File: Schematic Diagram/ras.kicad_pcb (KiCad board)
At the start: 2 copper layers, 1 part

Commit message: display parts
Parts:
- added BZ1: Buzzer, project:Buzzer_12x9.5RM7.6, F.Cu at (159.2, 32.4)
- added D1: LED_RED, project:LED_D5.0mm, F.Cu at (161.7, 54.7)
- added D2: LED_GREEN, project:LED_D5.0mm, F.Cu at (161.7, 48.3)
- added D3: LED_BLUE, project:LED_D5.0mm, F.Cu at (161.7, 41.9)
- added LCD_Module1: I2C_transport_LCD, project:WC1602A, F.Cu at (181.0, 27.4)
- added R1: 130Ω, project:R_Axial_DIN0207_L6.3mm_D2.5mm_P7.62mm_Horizontal, F.Cu at (170.8, 60.1)
- added R2: 130Ω, project:R_Axial_DIN0207_L6.3mm_D2.5mm_P7.62mm_Horizontal, F.Cu at (167.8, 60.1)
- added R3: 130Ω, project:R_Axial_DIN0207_L6.3mm_D2.5mm_P7.62mm_Horizontal, F.Cu at (164.8, 60.1)
- added RFID1: RC522, project:RFID-RC522, F.Cu at (241.7, 77.2)
- added SW1: SHUTDOWN, project:SW_PUSH_6mm, F.Cu at (156.8, 67.2)
- added SW2: HOME, project:SW_PUSH_6mm, F.Cu at (187.0, 65.2)
- added SW3: MENU, project:SW_PUSH_6mm, F.Cu at (194.5, 65.2)
- added SW4: PREVIOUS, project:SW_PUSH_6mm, F.Cu at (202.0, 65.2)
- added SW5: RotaryEncoder_Switch, project:RotaryEncoder_Alps_EC12E-Switch_Vertical_H20mm, F.Cu at (207.0, 66.0)
- added SW6: NEXT, project:SW_PUSH_6mm, F.Cu at (231.0, 65.2)
- added SW7: DONE, project:SW_PUSH_6mm, F.Cu at (250.8, 65.2)
- added U1: ~, project:DS3231M, B.Cu at (223.8, 25.3)
- RP1: footprint raspberrypi:raspberrypi_2_3 -> project:raspberrypi3
- moved RP1 98.2 mm to (230.9, 118.8)
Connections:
- RP1 pad 1: unconnected-(RP1-Pad1) -> +3V3
- RP1 pad 13: unconnected-(RP1-Pad13) -> LED-RED
- RP1 pad 14: unconnected-(RP1-Pad14) -> GND
- RP1 pad 15: unconnected-(RP1-Pad15) -> LED-GREEN
- RP1 pad 16: unconnected-(RP1-Pad16) -> LED-BLUE
- RP1 pad 18: unconnected-(RP1-Pad18) -> RFID-IRQ
- RP1 pad 19: unconnected-(RP1-Pad19) -> SPI_MOSI
- RP1 pad 2: unconnected-(RP1-Pad2) -> +5V
- RP1 pad 20: unconnected-(RP1-Pad20) -> GND
- RP1 pad 21: unconnected-(RP1-Pad21) -> SPI_MISO
- RP1 pad 22: unconnected-(RP1-Pad22) -> RFID-RST
- RP1 pad 23: unconnected-(RP1-Pad23) -> SPI_SCLK
- RP1 pad 24: unconnected-(RP1-Pad24) -> SPI_CE-RFID
- RP1 pad 25: unconnected-(RP1-Pad25) -> GND
- RP1 pad 29: unconnected-(RP1-Pad29) -> HOME_BUTTON
- RP1 pad 3: unconnected-(RP1-Pad3) -> I2C_SDA
- RP1 pad 30: unconnected-(RP1-Pad30) -> GND
- RP1 pad 31: unconnected-(RP1-Pad31) -> MENU_BUTTON
- RP1 pad 32: unconnected-(RP1-Pad32) -> Buzzer
- RP1 pad 33: unconnected-(RP1-Pad33) -> PREVIOUS_BUTTON
- RP1 pad 34: unconnected-(RP1-Pad34) -> GND
- RP1 pad 35: unconnected-(RP1-Pad35) -> DONE_BUTTON
- RP1 pad 37: unconnected-(RP1-Pad37) -> NEXT_BUTTON
- RP1 pad 38: unconnected-(RP1-Pad38) -> ENCODER_A
- RP1 pad 39: unconnected-(RP1-Pad39) -> GND
- RP1 pad 40: unconnected-(RP1-Pad40) -> ENCODER_B
- RP1 pad 5: unconnected-(RP1-Pad5) -> I2C_SCL
- RP1 pad 6: unconnected-(RP1-Pad6) -> GND
- RP1 pad 7: unconnected-(RP1-Pad7) -> SHUTDOWN_BUTTON
- RP1 pad 9: unconnected-(RP1-Pad9) -> GND

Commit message: wiring
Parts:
- moved R1 9.70 mm to (164.8, 67.7), turned to 90 degrees
- moved R3 9.70 mm to (170.8, 67.7), turned to 90 degrees
- moved R2 7.62 mm to (167.8, 67.7), turned to 90 degrees
- moved U1 1.50 mm to (225.3, 25.3)
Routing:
- net GND: track 0.00 -> 408.0 mm, vias 0 -> 89
- net +5V: track 0.00 -> 166.3 mm
- net I2C_SDA: track 0.00 -> 155.6 mm, vias 0 -> 2
- net I2C_SCL: track 0.00 -> 143.9 mm
- net LED-BLUE: track 0.00 -> 132.1 mm, vias 0 -> 1
- net Buzzer: track 0.00 -> 119.6 mm, vias 0 -> 1
- net DONE_BUTTON: track 0.00 -> 110.5 mm, vias 0 -> 2
- net SHUTDOWN_BUTTON: track 0.00 -> 94.1 mm, vias 0 -> 1
- net LED-RED: track 0.00 -> 93.5 mm, vias 0 -> 2
- net LED-GREEN: track 0.00 -> 90.8 mm, vias 0 -> 2
- net NEXT_BUTTON: track 0.00 -> 81.6 mm, vias 0 -> 1
- net ENCODER_A: track 0.00 -> 65.6 mm, vias 0 -> 1
- net SPI_CE-RFID: track 0.00 -> 64.7 mm, vias 0 -> 1
- net HOME_BUTTON: track 0.00 -> 63.9 mm, vias 0 -> 1
- net ENCODER_B: track 0.00 -> 63.9 mm, vias 0 -> 1
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- added copper zone on B.Cu, net GND
- added copper zone on F.Cu, net GND
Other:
- board outline added: 100 x 100 mm
- board text added: "PCB Designed by souchan.jp"

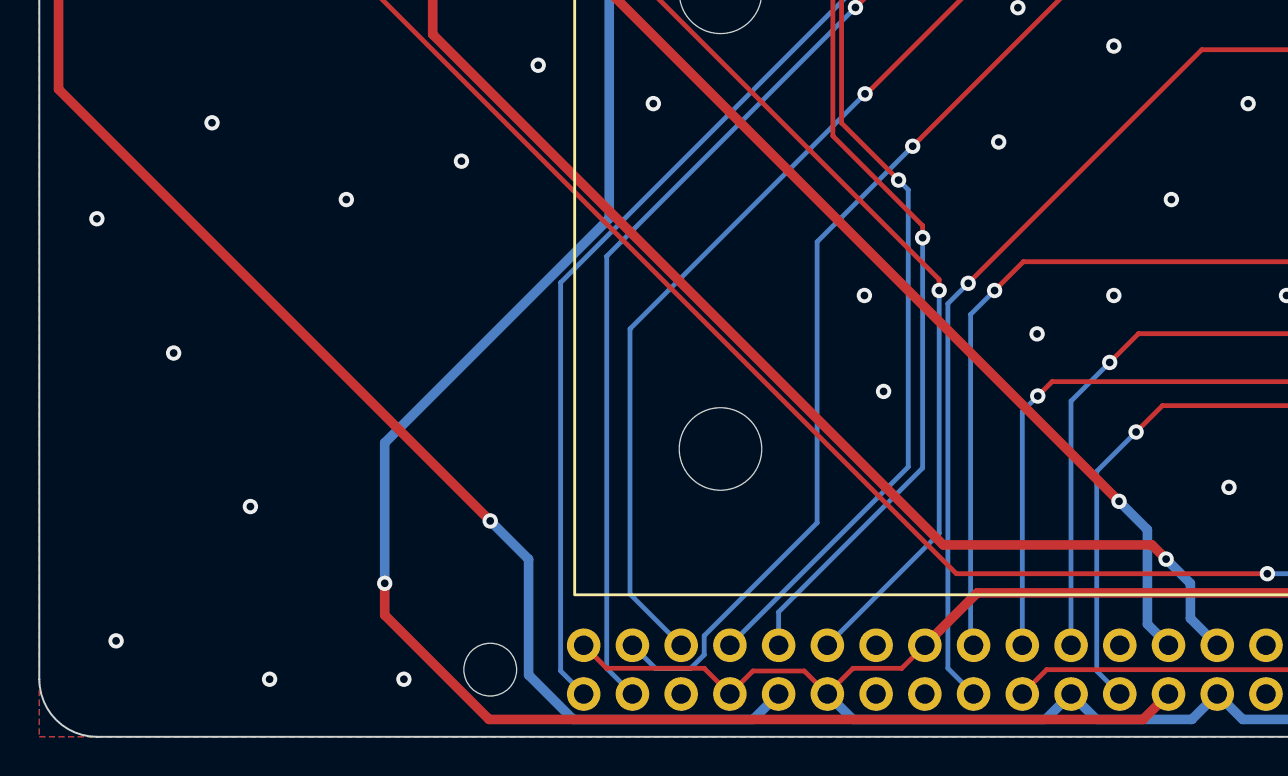
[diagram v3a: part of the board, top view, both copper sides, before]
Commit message: add logo
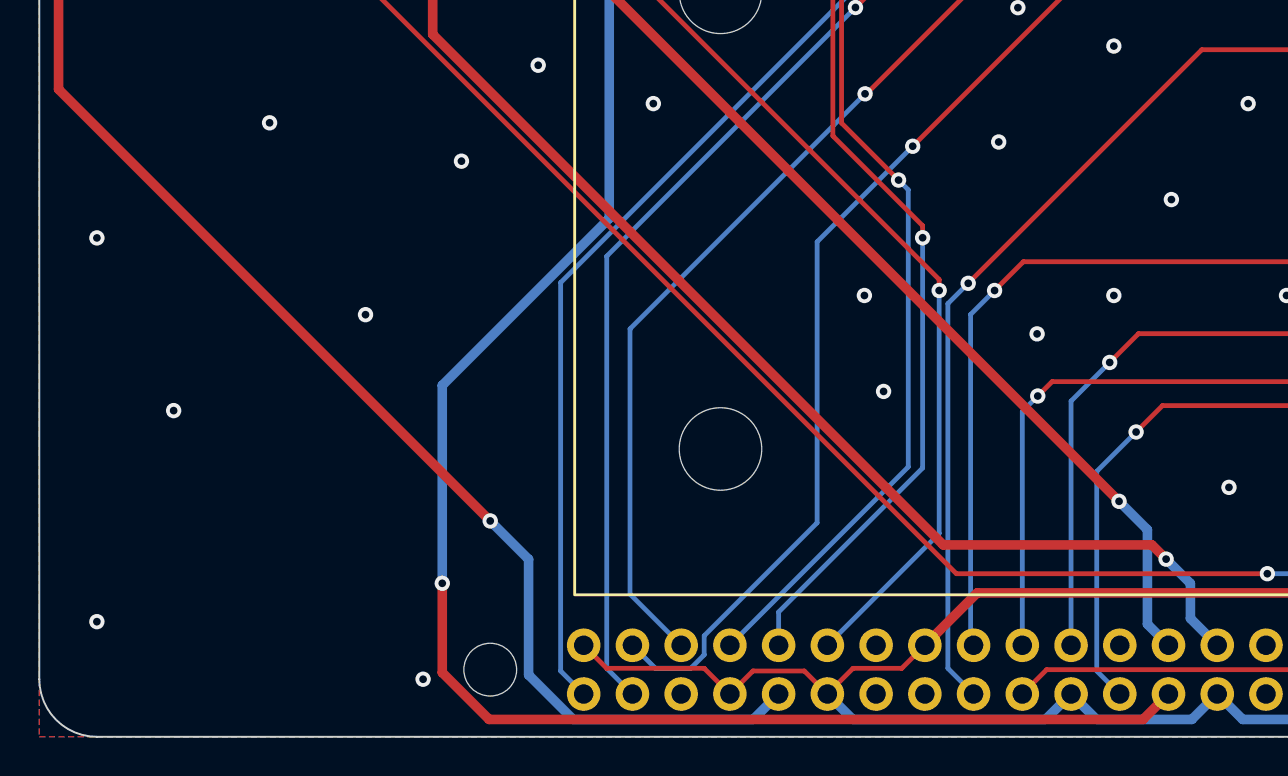
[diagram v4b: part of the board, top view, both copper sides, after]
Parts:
- added REF**: logo, project:logo, F.Cu at (166.3, 119.6)
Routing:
- net LED-BLUE: track 132.1 -> 129.6 mm
- net GND: vias 89 -> 87
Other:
- board text removed: "PCB Designed by souchan.jp"

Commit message: pass DRC checks
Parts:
- REF**: moved to B.Cu
- moved REF** 80.5 mm to (204.3, 48.6), turned to 180 degrees
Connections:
- RP1 pad 34: GND -> unconnected-(RP1-GND_7-Pad34)
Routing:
- net GND: track 408.0 -> 387.6 mm, vias 87 -> 73
- net SHUTDOWN_BUTTON: track 94.1 -> 107.0 mm, vias 1 -> 2
- net LED-BLUE: track 129.6 -> 122.9 mm
- net Buzzer: track 119.6 -> 115.8 mm, vias 1 -> 0
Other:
- outline, holes or cut-outs redrawn

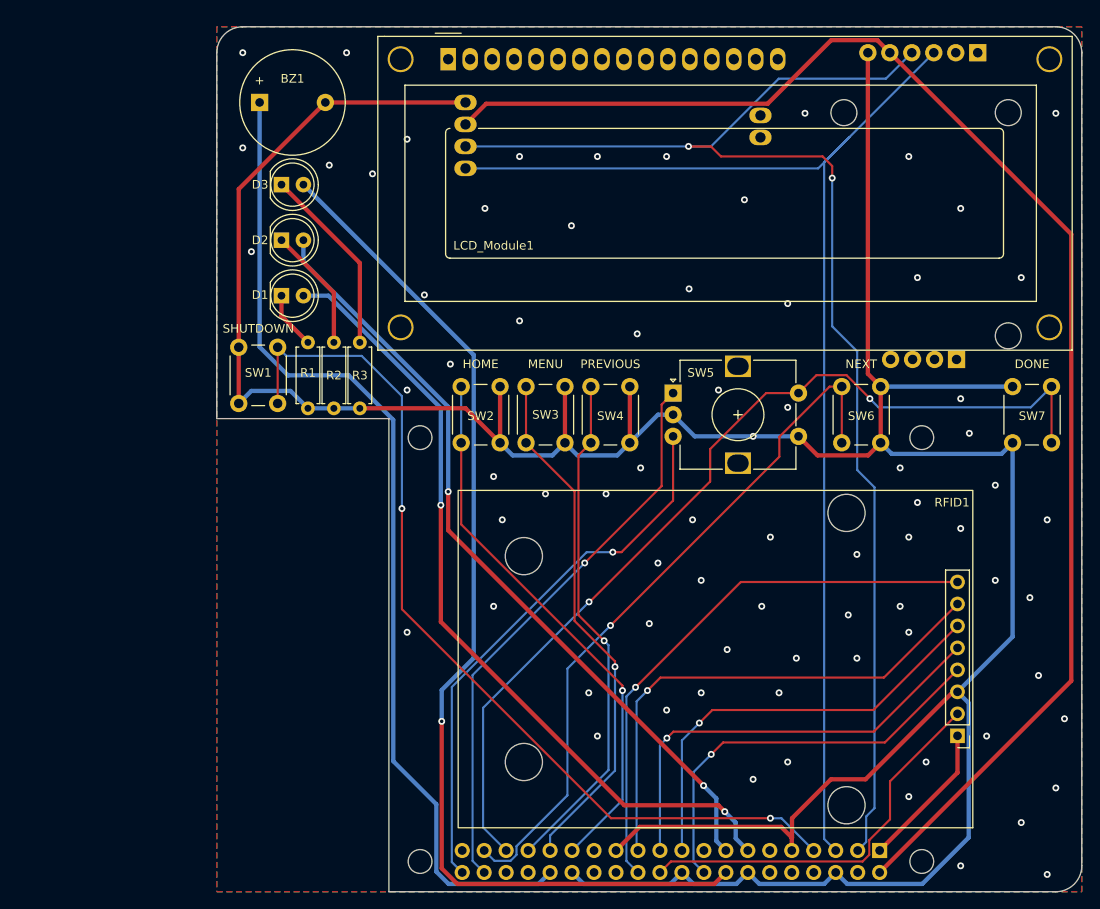
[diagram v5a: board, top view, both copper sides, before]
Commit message: fix PCB design (closed #7)
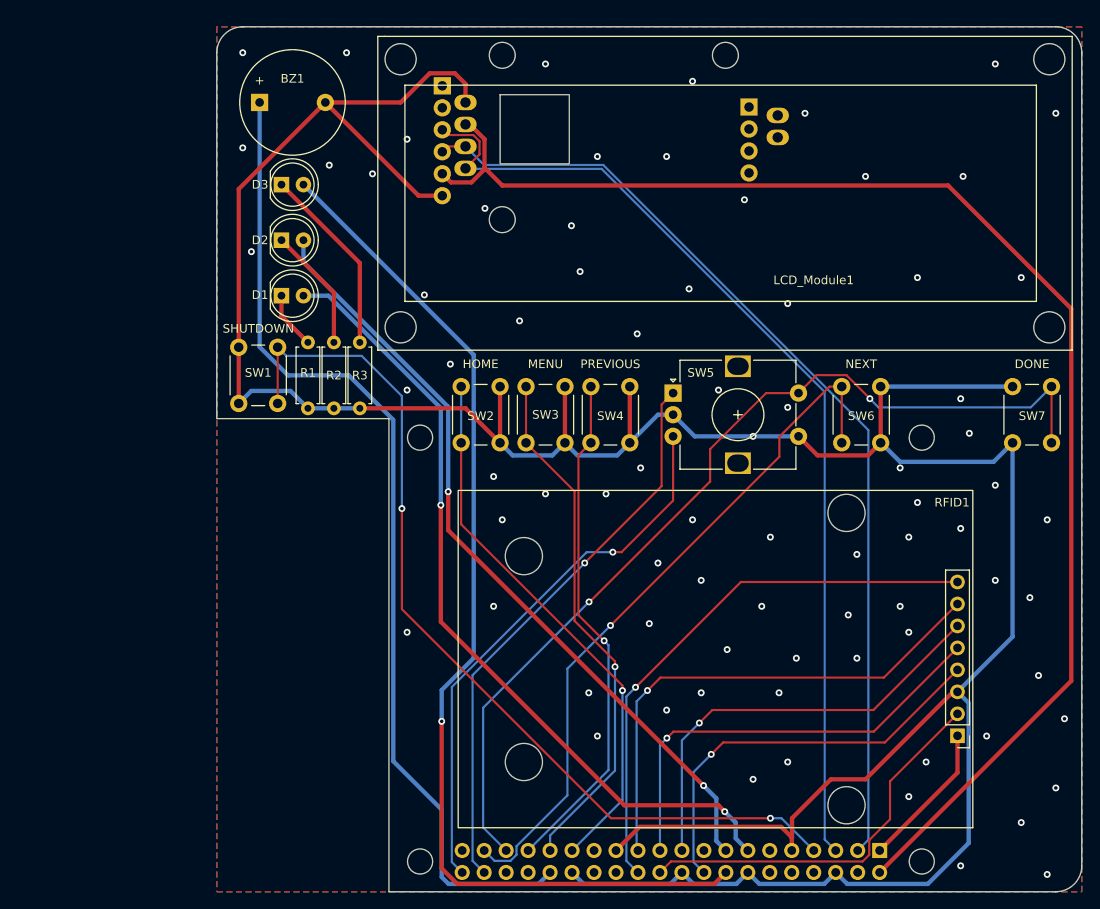
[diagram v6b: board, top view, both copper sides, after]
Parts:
- moved U1 51.2 mm to (179.1, 47.4), turned to 0 degrees
- moved REF** 37.9 mm to (238.3, 31.9)
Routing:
- net I2C_SDA: track 155.6 -> 112.2 mm, vias 2 -> 0
- net I2C_SCL: track 143.9 -> 114.4 mm
- net GND: track 387.6 -> 371.6 mm, vias 73 -> 76
- net +5V: track 166.3 -> 161.3 mm
